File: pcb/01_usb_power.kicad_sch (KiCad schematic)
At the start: 12 parts, among them U15 TLV1117LV33DCYR

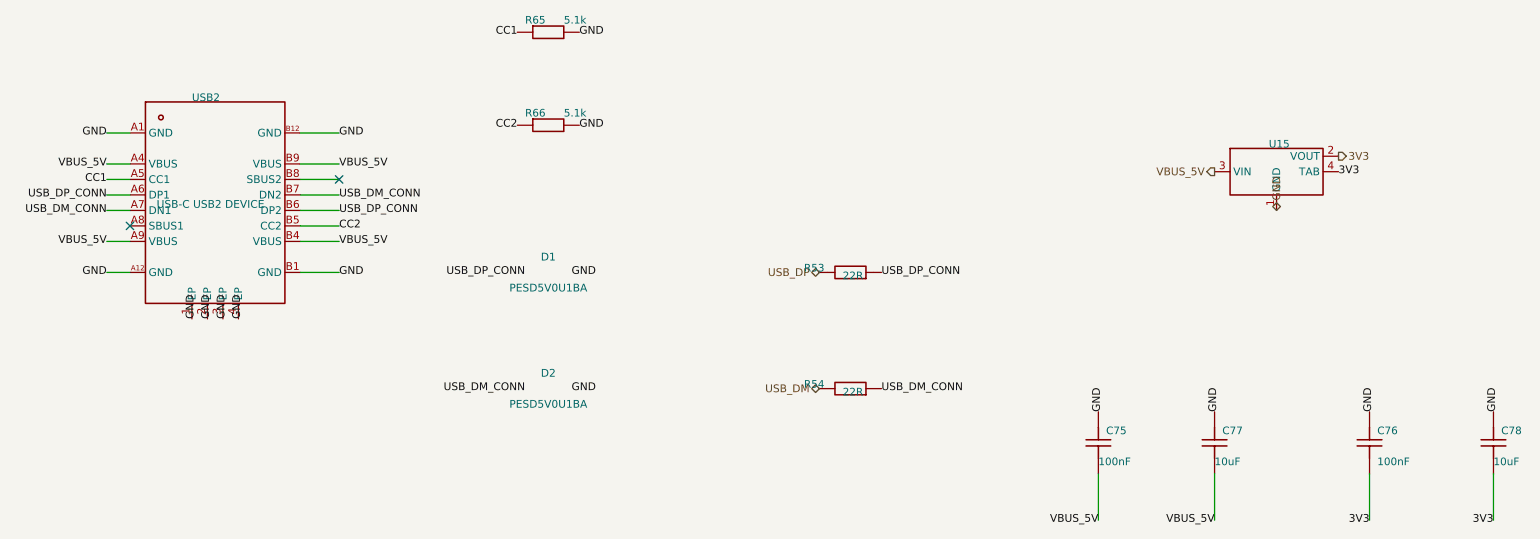
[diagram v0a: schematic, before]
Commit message: 修复原理图电源网络并更新项目文档
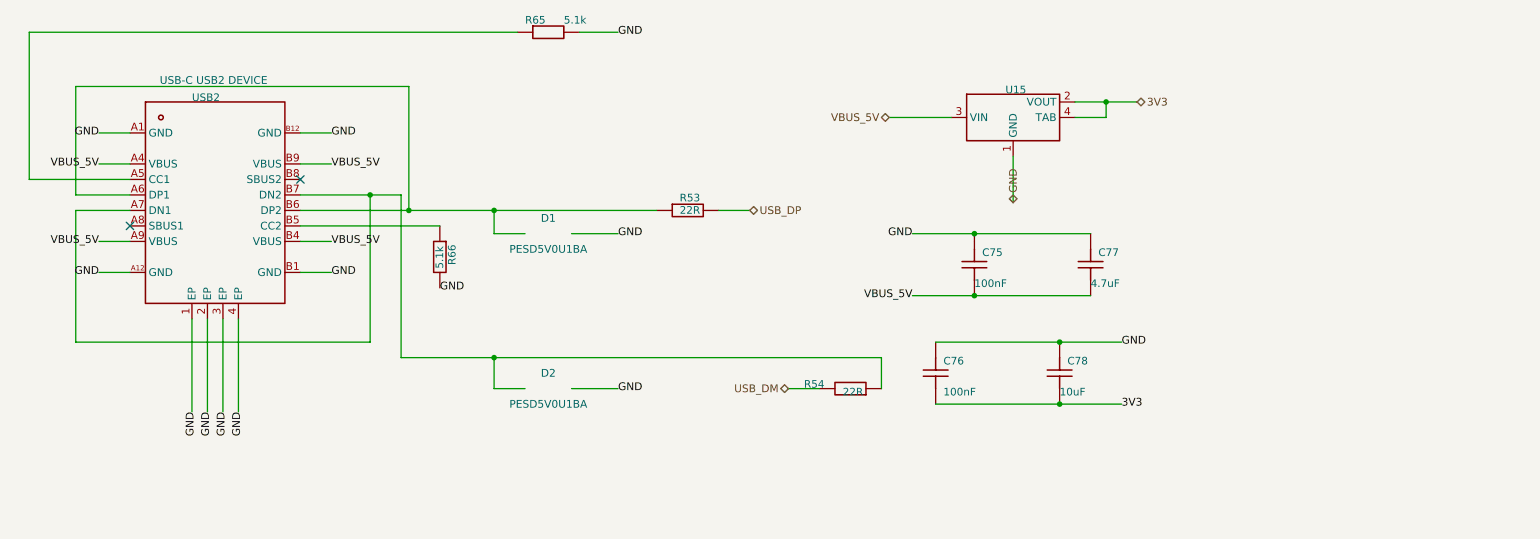
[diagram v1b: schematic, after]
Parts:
- C77: value 10uF -> 4.7uF; footprint Capacitor_SMD:C_0805_2012Metric -> Capacitor_SMD:C_0603_1608Metric
- C78: footprint Capacitor_SMD:C_0805_2012Metric -> Capacitor_SMD:C_0603_1608Metric
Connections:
- net CC1: no longer names the net of R65.1, USB2.A5 (CC1)
- net CC2: no longer names the net of R66.1, USB2.B5 (CC2)
- net USB_DM_CONN: no longer names the net of D2.1 (A1), R54.1, USB2.A7 (DN1), USB2.B7 (DN2)
- net USB_DP_CONN: no longer names the net of D1.1 (A1), R53.1, USB2.A6 (DP1), USB2.B6 (DP2)
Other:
- moved on the sheet: C75, C76, C77, C78, R53, R66, U15
